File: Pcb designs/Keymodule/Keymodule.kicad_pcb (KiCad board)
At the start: 4 copper layers, 91 x 91 mm, 115 parts, among them J3 Conn_01x03, J6 Conn_01x03, U1 RP2040, U2 SN74LV1T34DBV, U3 AMS1117-3.3, U4 W25Q128JVS, Y1 ABM8-272-T3

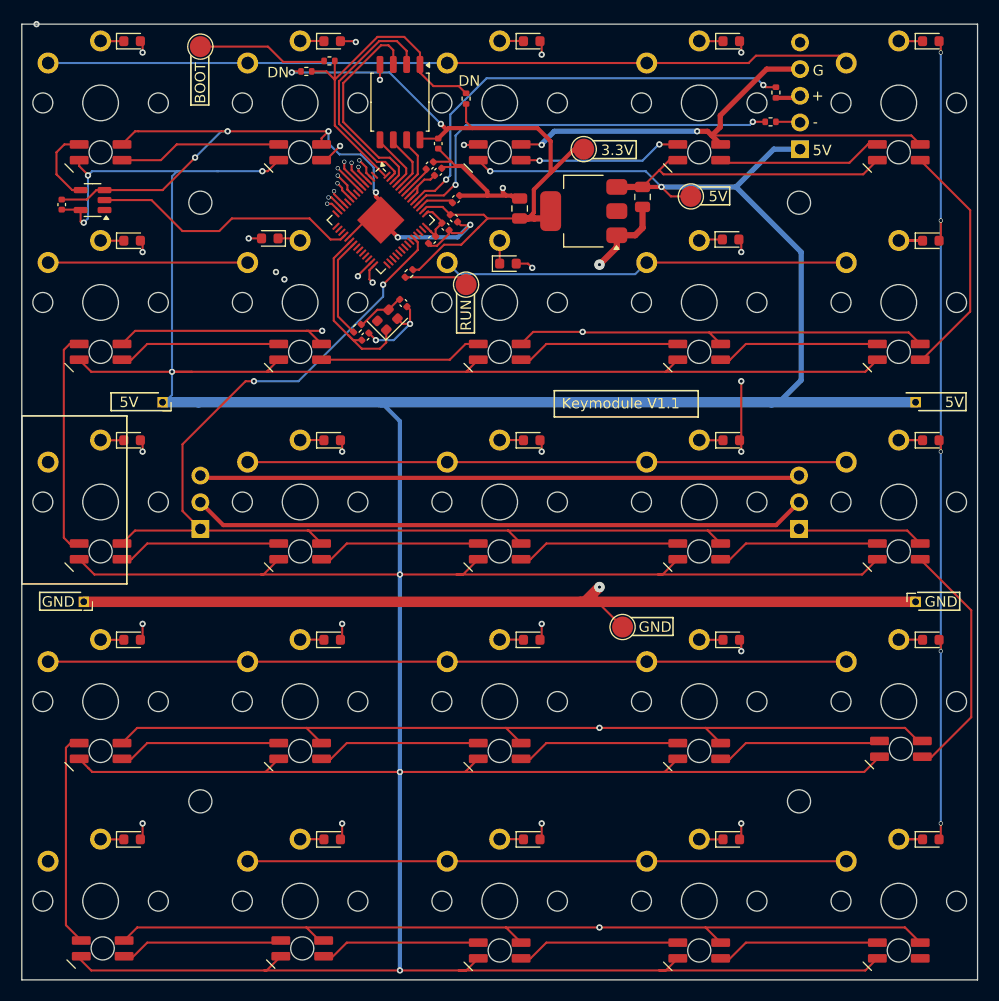
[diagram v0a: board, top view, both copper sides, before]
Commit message: Created main SW assembly
still needs lots of work
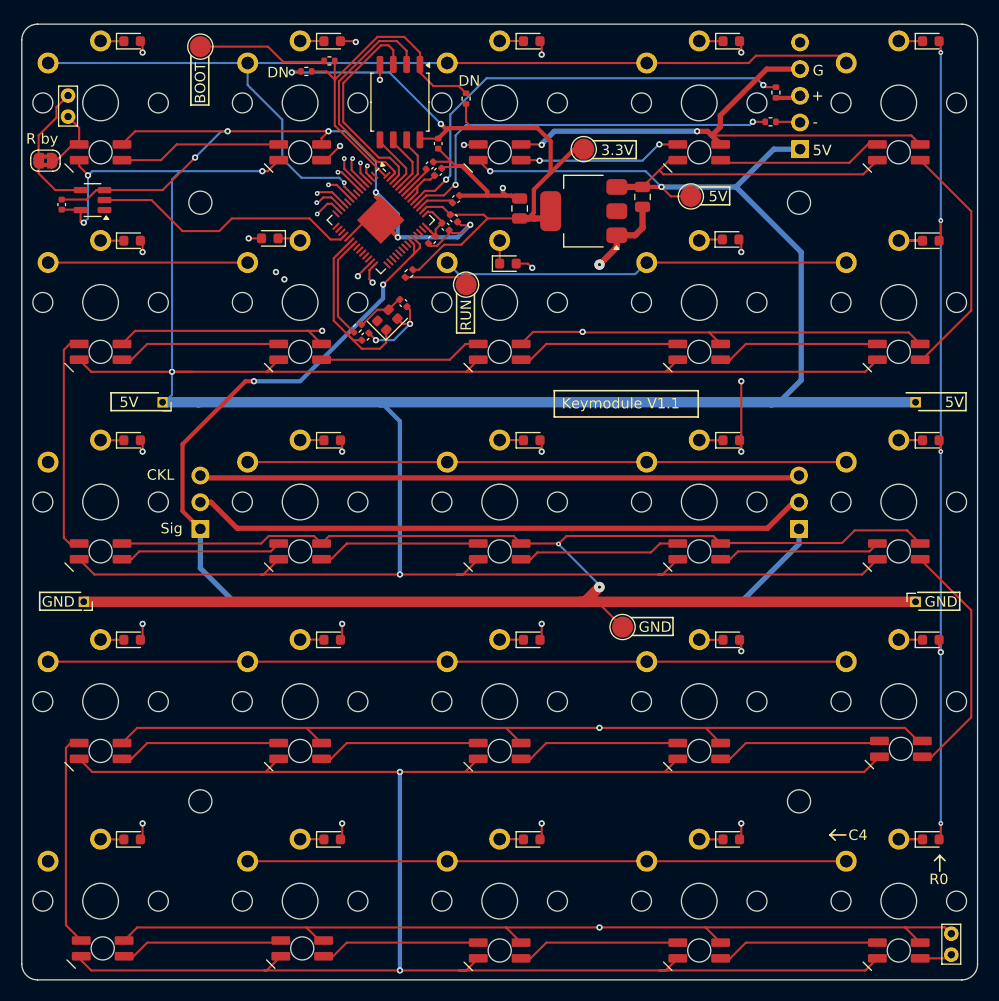
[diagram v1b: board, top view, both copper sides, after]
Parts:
- added REF**: TestPoint_Bridge_Pitch2.0mm_Drill0.7mm, TestPoint:TestPoint_Bridge_Pitch2.0mm_Drill0.7mm, F.Cu at (58.9, 61.3)
- added REF**: TestPoint_Bridge_Pitch2.0mm_Drill0.7mm, TestPoint:TestPoint_Bridge_Pitch2.0mm_Drill0.7mm, F.Cu at (143.0, 141.1)
- added REF**: SolderJumper-2_P1.3mm_Bridged2Bar_RoundedPad1.0x1.5mm, Jumper:SolderJumper-2_P1.3mm_Bridged2Bar_RoundedPad1.0x1.5mm, F.Cu at (56.8, 67.5)
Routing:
- net potSig: track 40.7 -> 109.2 mm
- net WS2812bData: track 7.49 -> 19.1 mm
- net GND: track 766.1 -> 772.8 mm, vias 18 -> 19
- net row3: track 99.0 -> 104.0 mm
- net unconnected-(L25-DOUT-Pad2): track 0.00 -> 3.10 mm
- net col2: track 108.0 -> 109.9 mm
- net row1: track 120.6 -> 118.7 mm
- net +5V: track 604.0 -> 602.6 mm
- net col3: track 126.6 -> 127.9 mm
- net SCL: track 90.4 -> 89.2 mm
- net row0: track 143.9 -> 144.8 mm
- net col4: track 144.7 -> 145.5 mm
- net (no net): vias 1 -> 0
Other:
- outline, holes or cut-outs redrawn
- board text added: "C4"
- board text added: "CKL"
- board text added: "R by"
- board text added: "R0"
- board text added: "Sig"

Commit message: Ihope this is the one
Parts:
- removed C12, C9: 1uf, Capacitor_SMD:C_0402_1005Metric
- added C4: 100nf, Capacitor_SMD:C_0402_1005Metric, F.Cu at (82.9, 76.6)
- added C4: 100nf, Capacitor_SMD:C_0402_1005Metric, F.Cu at (80.5, 71.8)
- added REF**: C_0603_1608Metric, Capacitor_SMD:C_0603_1608Metric, F.Cu at (96.6, 70.4)
- added REF**: C_0603_1608Metric, Capacitor_SMD:C_0603_1608Metric, F.Cu at (96.0, 73.1)
- added REF**: SW_PUSH_6mm, Button_Switch_THT:SW_PUSH_6mm, F.Cu at (71.4, 112.8)
- moved 5V 7.50 mm to (60.4, 90.5)
- moved D4 3.36 mm to (138.8, 77.6)
- moved C8 3.28 mm to (92.1, 78.0), turned to -45 degrees
- moved D6 3.28 mm to (138.7, 115.4)
- moved R4 1.90 mm to (92.4, 79.9), turned to 135 degrees
- moved C11 0.32 mm to (93.3, 67.6), turned to -45 degrees
- moved C5 0.14 mm to (94.3, 68.6)
- moved RUN 0.10 mm to (96.9, 79.3)
- renumbered DN to NO
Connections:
- Y1 pad 4: unconnected-(Y1-Vdd-Pad4) -> GND
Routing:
- net Net-(U1-ADC_AVDD): track 9.42 -> 74.4 mm, vias 0 -> 6
- net GND: track 772.8 -> 751.0 mm, vias 19 -> 23
- net +1V1: track 6.50 -> 23.6 mm, vias 0 -> 3
- net +3.3V: track 67.9 -> 58.7 mm
- net /run: track 6.30 -> 15.4 mm
- net +5V: track 602.6 -> 610.0 mm
- net row0: track 144.8 -> 147.7 mm
- net Net-(L10-DOUT): track 23.0 -> 20.2 mm
- net Net-(L15-DOUT): track 23.3 -> 20.6 mm
- net Net-(D4-K): track 4.50 -> 2.50 mm
- net SCL: track 89.2 -> 88.0 mm, vias 2 -> 1
- net SDA: track 95.3 -> 94.3 mm, vias 2 -> 1
- net col1: track 93.8 -> 94.5 mm
- net potSig: track 109.2 -> 110.0 mm
- net WS2812bData: track 19.1 -> 18.5 mm
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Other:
- board text added: "1 uF"
- board text added: "Banana 1"
- board text added: "SOC"
- board text removed: "Keymodule V1.1"

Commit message: PCB is orderd !
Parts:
- added REF**: SolderJumper-2_P1.3mm_Bridged2Bar_RoundedPad1.0x1.5mm, Jumper:SolderJumper-2_P1.3mm_Bridged2Bar_RoundedPad1.0x1.5mm, F.Cu at (106.0, 77.3)
- moved RESET 46.2 mm to (113.1, 92.8), turned to 180 degrees
- moved R4 15.7 mm to (108.1, 80.1), turned to 90 degrees
- renumbered REF** to RESET
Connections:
- RESET pad 1: (no net) -> GND
- RESET pad 2: (no net) -> /run
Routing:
- net /run: track 15.4 -> 41.1 mm, vias 0 -> 2
- net GND: track 751.0 -> 775.8 mm
- net +3.3V: track 58.7 -> 76.7 mm
- net Net-(U1-ADC_AVDD): track 74.4 -> 73.3 mm
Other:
- board text added: "1"
- board text removed: "Banana 1"
